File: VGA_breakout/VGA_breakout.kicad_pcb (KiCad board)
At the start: 2 copper layers, 31.8 x 45.7 mm, 6 parts, among them J1 Breadboard connector, J2 VGA Port, J3 Holder2, J4 Holder1

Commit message: Small changes, generated gerber files
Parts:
- renumbered J2 to J1, J1 to J2
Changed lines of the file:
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@@
     (pcbplotparams
       (layerselection 0x010fc_ffffffff)
-      (usegerberextensions false)
+      (usegerberextensions true)
       (usegerberattributes false)
       (usegerberadvancedattributes false)
@@
       (outputformat 1)
       (mirror false)
-      (drillshape 1)
+      (drillshape 0)
       (scaleselection 1)
-      (outputdirectory ""))
+      (outputdirectory "gerbers/"))
   )
   (net 0 "")
@@
   (net 14 "Net-(J1-Pad2)")
   (net 15 "Net-(J1-Pad1)")
-  (net 16 "Net-(J2-Pad0)")
-  (net 17 "Net-(J3-Pad2)")
-  (net 18 "Net-(J3-Pad1)")
-  (net 19 "Net-(J4-Pad2)")
-  (net 20 "Net-(J4-Pad1)")
+  (net 16 "Net-(J3-Pad2)")
+  (net 17 "Net-(J3-Pad1)")
+  (net 18 "Net-(J4-Pad2)")
+  (net 19 "Net-(J4-Pad1)")
+  (net 20 "Net-(J1-Pad0)")
   (net_class Default "This is the default net class."
     (clearance 0.2)
@@
     (uvia_dia 0.3)
     (uvia_drill 0.1)
+    (add_net "Net-(J1-Pad0)")
     (add_net "Net-(J1-Pad1)")
     (add_net "Net-(J1-Pad10)")
@@
     (add_net "Net-(J1-Pad8)")
     (add_net "Net-(J1-Pad9)")
-    (add_net "Net-(J2-Pad0)")
     (add_net "Net-(J3-Pad1)")
     (add_net "Net-(J3-Pad2)")
@@
     (fp_line (start -0.635 1.27) (end 1.27 1.27) (layer B.Fab) (width 0.1))
     (pad 2 thru_hole oval (at 0 -2.54 270) (size 1.7 1.7) (drill 1) (layers *.Cu *.Mask)
-      (net 19 "Net-(J4-Pad2)"))
+      (net 18 "Net-(J4-Pad2)"))
     (pad 1 thru_hole rect (at 0 0 270) (size 1.7 1.7) (drill 1) (layers *.Cu *.Mask)
-      (net 20 "Net-(J4-Pad1)"))
+      (net 19 "Net-(J4-Pad1)"))
     (model ${KISYS3DMOD}/Connector_PinHeader_2.54mm.3dshapes/PinHeader_1x02_P2.54mm_Vertical.wrl
       (at (xyz 0 0 0))
@@
     (fp_line (start -0.635 1.27) (end 1.27 1.27) (layer B.Fab) (width 0.1))
     (pad 2 thru_hole oval (at 0 -2.54 270) (size 1.7 1.7) (drill 1) (layers *.Cu *.Mask)
-      (net 17 "Net-(J3-Pad2)"))
+      (net 16 "Net-(J3-Pad2)"))
     (pad 1 thru_hole rect (at 0 0 270) (size 1.7 1.7) (drill 1) (layers *.Cu *.Mask)
-      (net 18 "Net-(J3-Pad1)"))
+      (net 17 "Net-(J3-Pad1)"))
     (model ${KISYS3DMOD}/Connector_PinHeader_2.54mm.3dshapes/PinHeader_1x02_P2.54mm_Vertical.wrl
       (at (xyz 0 0 0))
@@
     (descr "15-pin D-Sub connector, horizontal/angled (90 deg), THT-mount, female, pitch 2.29x1.98mm, pin-PCB-offset 8.35mm, distance of mounting holes 25mm, distance of mounting holes to PCB edge 10.889999999999999mm, see https://disti-assets.s3.amazonaws.com/tonar/files/datasheets/16730.pdf")
     (tags "15-pin D-Sub connector horizontal angled 90deg THT female pitch 2.29x1.98mm pin-PCB-offset 8.35mm mounting-holes-distance 25mm mounting-hole-offset 25mm")
-    (fp_text reference J2 (at -4.315 -2.58 90) (layer F.SilkS)
+    (fp_text reference J1 (at -4.315 -2.58 90) (layer F.SilkS)
       (effects (font (size 1 1) (thickness 0.15)))
     )
@@
     (fp_arc (start -16.815 1.42) (end -18.415 1.42) (angle 180) (layer F.Fab) (width 0.1))
     (pad 0 thru_hole circle (at 8.185 1.42 90) (size 4 4) (drill 3.2) (layers *.Cu *.Mask)
-      (net 16 "Net-(J2-Pad0)"))
+      (net 20 "Net-(J1-Pad0)"))
     (pad 0 thru_hole circle (at -16.815 1.42 90) (size 4 4) (drill 3.2) (layers *.Cu *.Mask)
-      (net 16 "Net-(J2-Pad0)"))
+      (net 20 "Net-(J1-Pad0)"))
     (pad 15 thru_hole circle (at -9.16 3.96 90) (size 1.6 1.6) (drill 1) (layers *.Cu *.Mask)
       (net 1 "Net-(J1-Pad15)"))
@@
     (descr "Through hole straight pin header, 1x15, 2.54mm pitch, single row")
     (tags "Through hole pin header THT 1x15 2.54mm single row")
-    (fp_text reference J1 (at 0 2.33) (layer B.SilkS)
-      (effects (font (size 1 1) (thickness 0.15)) (justify mirror))
-    )
+    (fp_text reference J2 (at 0 2.33) (layer B.SilkS) hide
+      (effects (font (size 1 1) (thickness 0.15)) (justify mirror))
+    )

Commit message: Cosmetic changes to VGA breakout board
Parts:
- added REF**: KiCad-Logo2_5mm_SilkScreen, Symbol:KiCad-Logo2_5mm_SilkScreen, B.Cu at (133.3, 88.9)
- added REF**: OSHW-Logo2_7.3x6mm_SilkScreen, Symbol:OSHW-Logo2_7.3x6mm_SilkScreen, B.Cu at (151.1, 88.9)
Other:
- board text added: "Author: Dawid Buchwald"
- board text added: "J2"
- board text added: "VGA Breadboard Breakout Board"

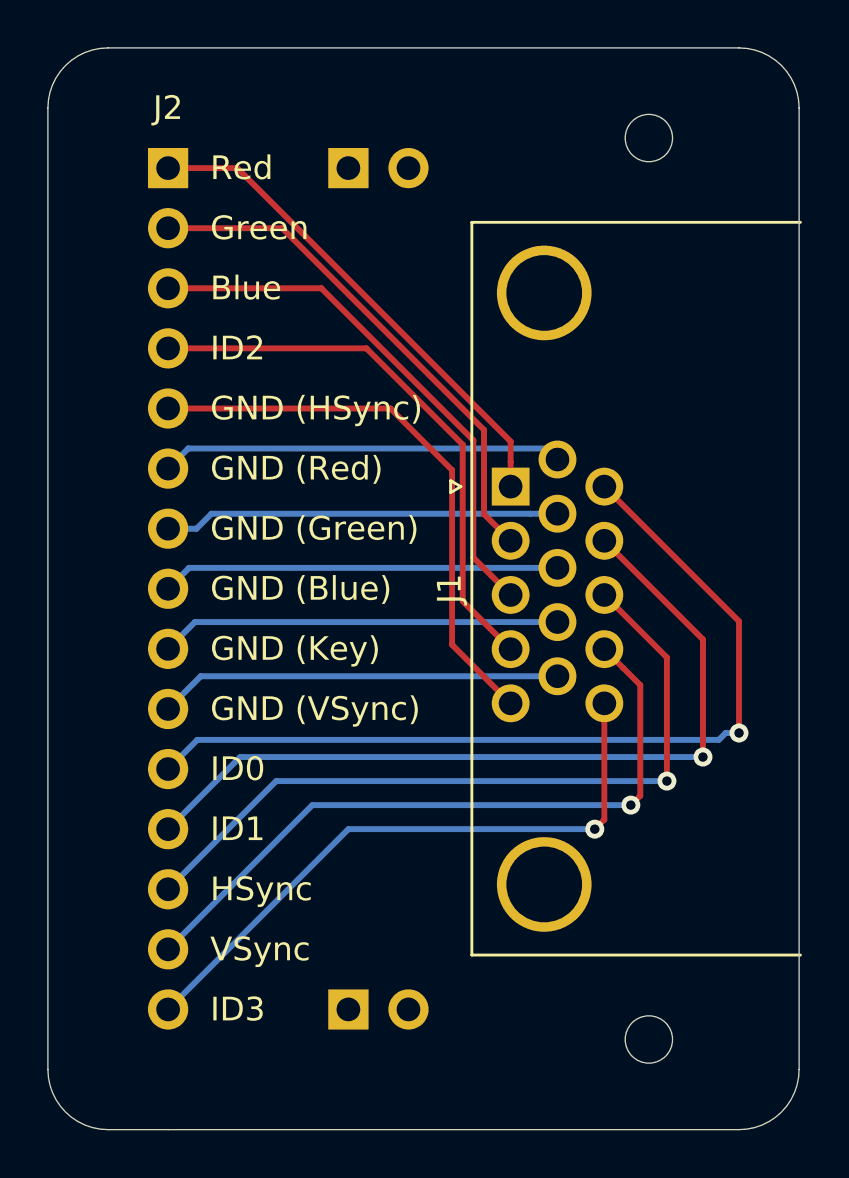
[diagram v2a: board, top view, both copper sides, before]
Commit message: Corrected VGA breakout board DSUB-15 footprint
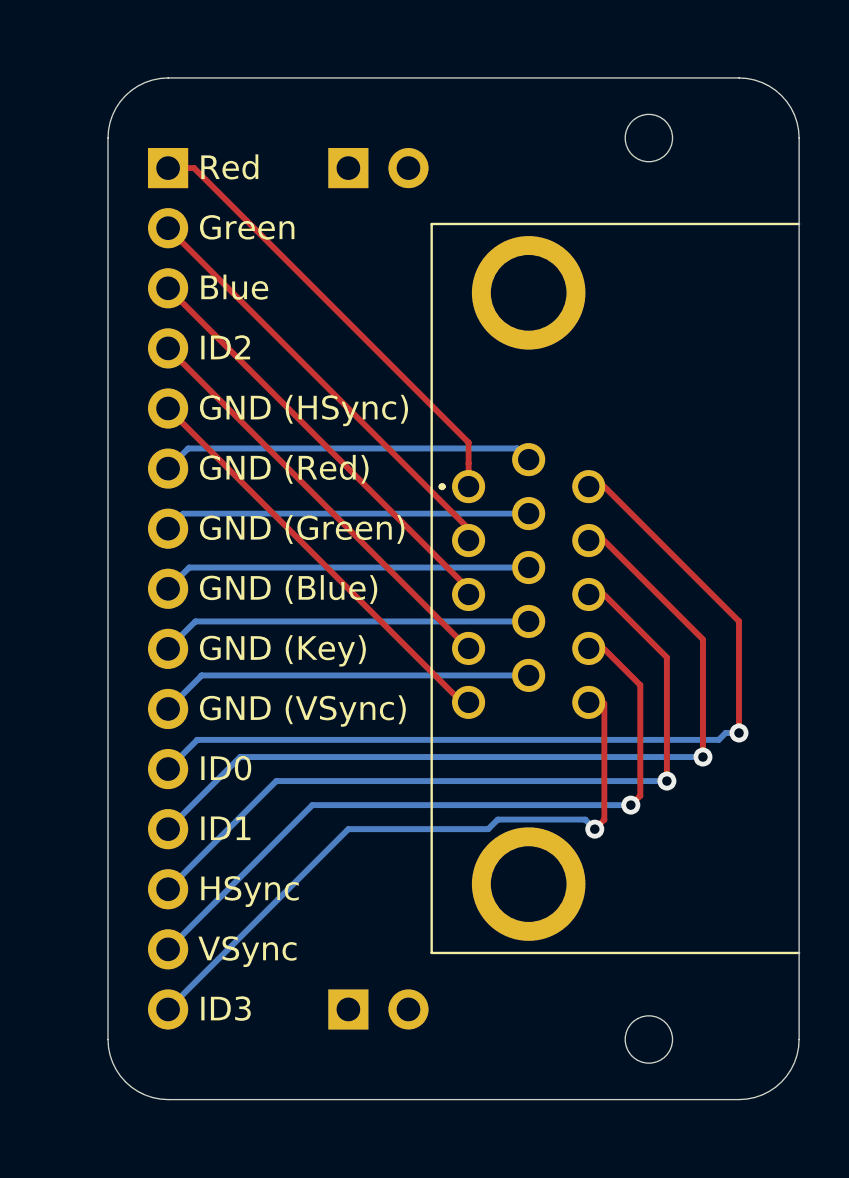
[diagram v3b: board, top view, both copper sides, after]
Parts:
- J1: footprint Connector_Dsub:DSUB-15-HD_Female_Horizontal_P2.29x1.98mm_EdgePinOffset8.35mm_Housed_MountingHolesOffset10.89mm -> VGA_breakout:ICD15S13E4GV00LF
- moved REF** 18.1 mm to (151.1, 85.3)
- moved REF** 12.2 mm to (151.1, 101.1)
- moved J1 1.78 mm to (141.0, 84.6)
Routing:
- net Net-(J1-Pad5): track 24.0 -> 17.8 mm
- net Net-(J1-Pad4): track 23.6 -> 18.0 mm
- net Net-(J1-Pad3): track 22.8 -> 18.2 mm
- net Net-(J1-Pad2): track 22.0 -> 18.5 mm
- net Net-(J1-Pad1): track 21.2 -> 19.4 mm
- net Net-(J1-Pad6): track 17.0 -> 15.8 mm
- net Net-(J1-Pad8): track 16.8 -> 15.6 mm
- net Net-(J1-Pad9): track 16.9 -> 15.7 mm
- net Net-(J1-Pad10): track 17.0 -> 15.8 mm
- net Net-(J1-Pad7): track 16.7 -> 15.6 mm
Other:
- board size 31.8 x 45.7 mm -> 29.2 x 43.2 mm
- board text removed: "J2"
